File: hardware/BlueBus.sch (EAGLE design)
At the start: 139 parts, among them Q1 NMOSFET-BSS138K, Q2 PMOSFET-DMP32D4S, Q3 NMOSFET-BSS138K, X1 CRYSTAL-12MHZ

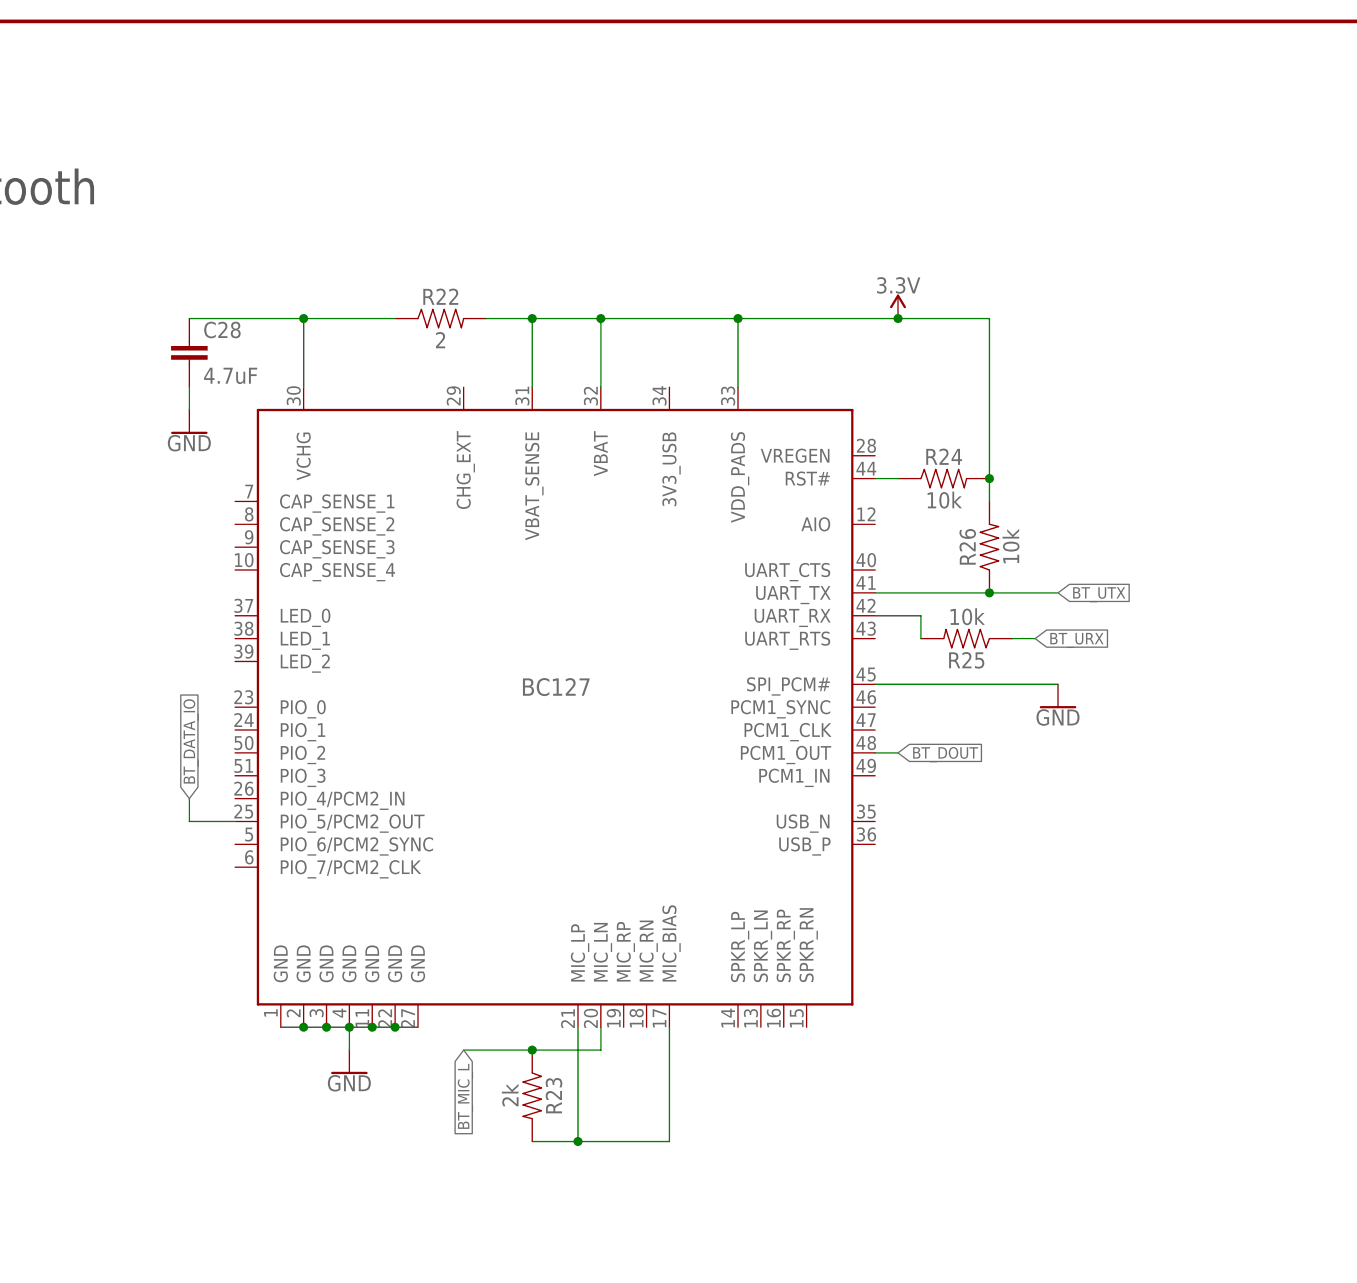
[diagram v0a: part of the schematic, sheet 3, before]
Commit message: [IMP] hardware: v1.1.6 * Re-wire BC127 power input for use with fixed regulated voltage, rather than battery power
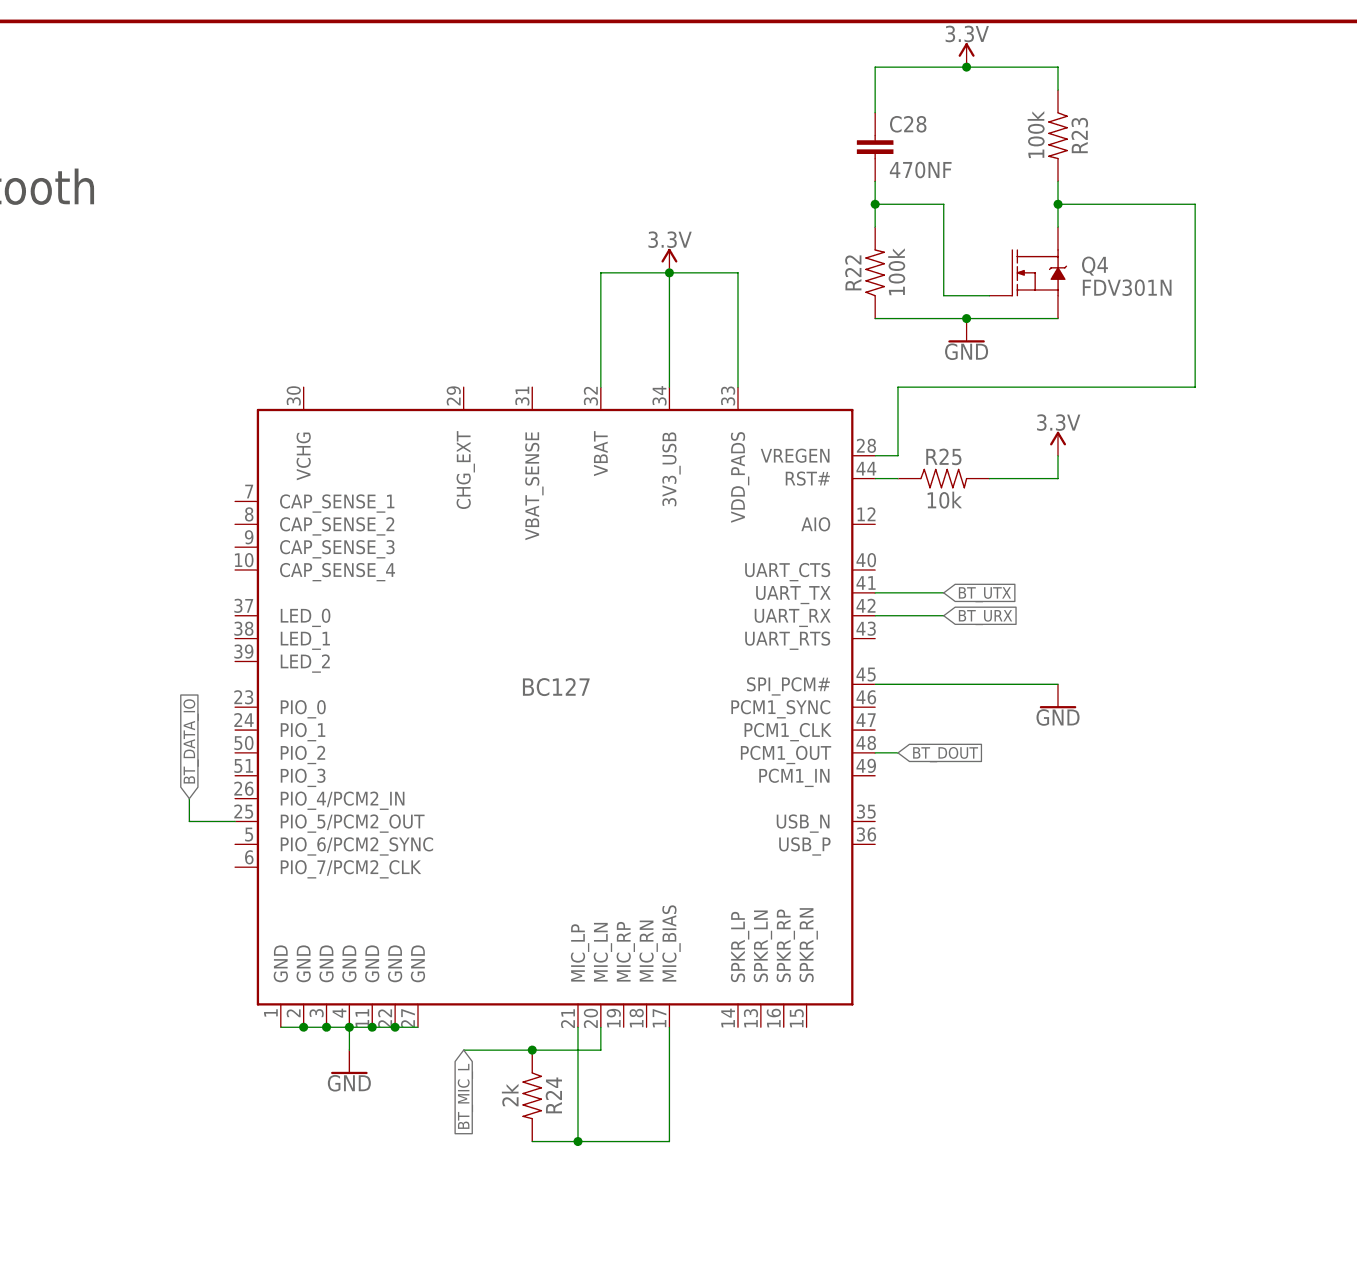
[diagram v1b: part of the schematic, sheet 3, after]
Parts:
- removed R38: 100, Passives:100OHM
- added Q4: FDV301N, Passives:FDV301N
- C28: value 4.7uF -> 470NF; device Passives:4.7UF -> Passives:470NF
- H1, H2, H3, H4: value 2,0-PAD -> 2,2-PAD; device Connectors:2,0-PAD -> Connectors:2,2-PAD
- R22: value 2 -> 100k; device Passives:2OHM -> Passives:100KOHM
- R23: value 2k -> 100k; device Passives:2KOHM -> Passives:100KOHM
- R24: value 10k -> 2k; device Passives:10KOHM -> Passives:2KOHM
- R26: value 10k -> 110; device Passives:10KOHM -> Passives:110OHM
- R27: value 110 -> 210; device Passives:110OHM -> Passives:210OHM
- R28: value 210 -> 10k; device Passives:210OHM -> Passives:10KOHM
- R29, R31: value 10k -> 4.7k; device Passives:10KOHM -> Passives:4.7KOHM
- R30, R32: value 4.7k -> 10k; device Passives:4.7KOHM -> Passives:10KOHM
- R33: value 10k -> 75; device Passives:10KOHM -> Passives:75OHM
- R34: value 75 -> 4.7k; device Passives:75OHM -> Passives:4.7KOHM
- R35: value 4.7k -> 18k; device Passives:4.7KOHM -> Passives:18KOHM
- R36: value 18k -> 100; device Passives:18KOHM -> Passives:100OHM
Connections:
- removed net BT_3V3_FILTER: BC127.VCHG, C28.1, R22.1
- removed net BT_URX_RES: BC127.UART_RX, R25.2
- new net BT_VREGEN: BC127.VREGEN, Q4.D, R23.2
- new net BT_VREGEN_CAP_GATE: C28.2, Q4.G, R22.2
- net 12V: now also R34.1; no longer R35.1
- net 3.3V: now also BC127.3V3_USB, C28.1, R23.1, R25.2, R28.1, R31.1; no longer BC127.VBAT_SENSE, R22.2, R24.2, R26.2, R30.1, R32.1
- net BT_DOUT: now also R33.2; no longer R34.2
- net BT_MIC_BIAS: now also R24.2; no longer R23.2
- net BT_MIC_L: now also R24.1; no longer R23.1
- net BT_RST: now also R25.1; no longer R24.1
- net BT_URX: now also BC127.UART_RX; no longer R25.1
- net BT_UTX: no longer R26.1
- net DAC_OUT_L: now also R37.1; no longer R38.1
- net DAC_OUT_R: now also R36.1; no longer R37.1
- net GND: now also Q4.S, R22.1, R26.1, R30.1, R32.1; no longer C28.2, R27.1, R31.1, R34.1
- net MCU_SCK3: now also R31.2; no longer R32.2
- net MCU_SDA3: now also R29.2; no longer R30.2
- net SPKR_OUT_L: now also R37.2; no longer R38.2
- net SPKR_OUT_R: now also R36.2; no longer R37.2
- net TEL_AMP_INL: now also R35.2; no longer R36.2
- net TEL_AMP_INL_CAP_RES: now also R35.1; no longer R36.1
- net TEL_MIC_L_OUT: now also R34.2; no longer R35.2
- net WM_CSB: now also R32.2; no longer R33.2
- net WM_GPO0: now also R30.2; no longer R31.2
- net WM_RESETB: now also R28.2; no longer R29.2
- net WM_SPDIF_TX_RES: now also R27.2; no longer R28.2
- net WM_SPDIF_TX_RES2: now also R26.2, R27.1; no longer R27.2, R28.1
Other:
- moved on the sheet: C28, R22, R23, R24, R25, R27, R28, R29, R30, R31, R32, R33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

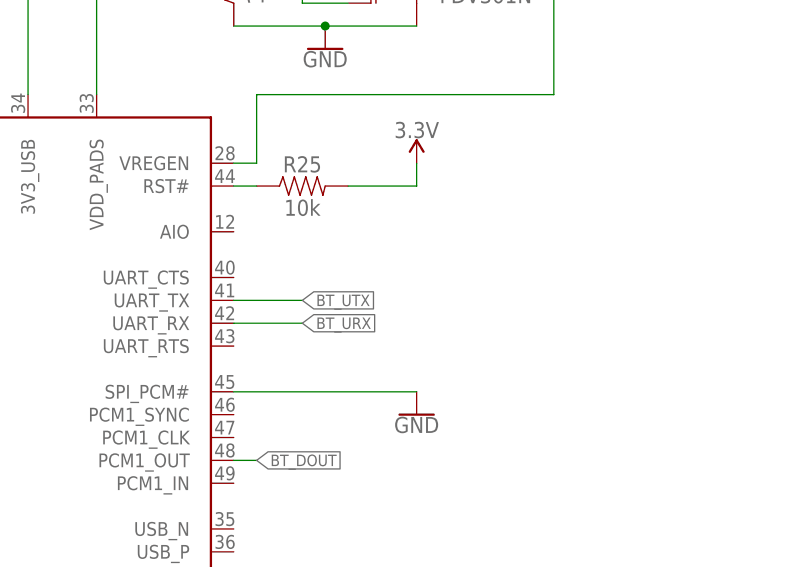
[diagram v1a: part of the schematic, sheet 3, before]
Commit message: [IMP] hardware: v1.6: Minor updates * Re-add 10k resistors to BC127 UART lines * Minor rewiring work around the TMUX154
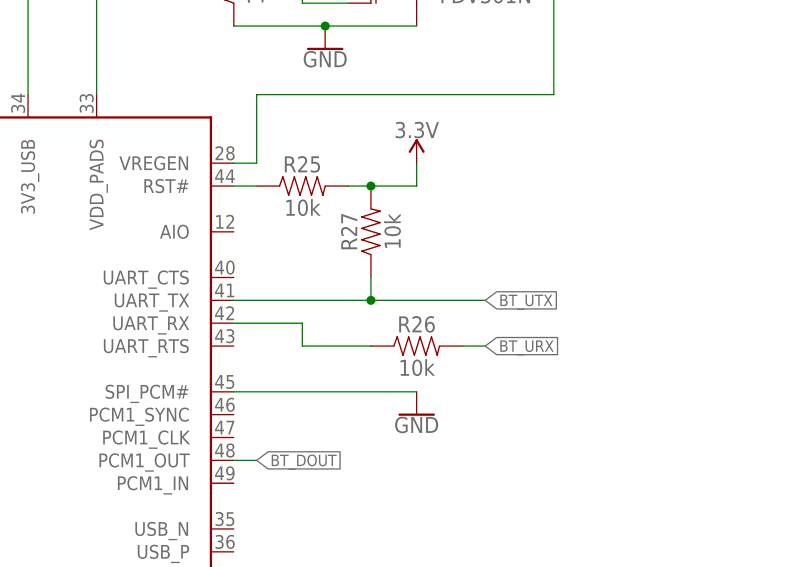
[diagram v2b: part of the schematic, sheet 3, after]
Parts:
- added R38, R39: 100, Passives:100OHM
- R26: value 110 -> 10k; device Passives:110OHM -> Passives:10KOHM
- R27: value 210 -> 10k; device Passives:210OHM -> Passives:10KOHM
- R28: value 10k -> 110; device Passives:10KOHM -> Passives:110OHM
- R29: value 4.7k -> 210; device Passives:4.7KOHM -> Passives:210OHM
- R33: value 75 -> 4.7k; device Passives:75OHM -> Passives:4.7KOHM
- R34: value 4.7k -> 10k; device Passives:4.7KOHM -> Passives:10KOHM
- R35: value 18k -> 75; device Passives:18KOHM -> Passives:75OHM
- R36: value 100 -> 4.7k; device Passives:100OHM -> Passives:4.7KOHM
- R37: value 100 -> 18k; device Passives:100OHM -> Passives:18KOHM
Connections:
- new net BT_URX_RES: BC127.UART_RX, R26.1
- net 12V: now also R36.1; no longer R34.1
- net 3.3V: now also R27.2, R30.1, R33.1; no longer R28.1, R29.1
- net BT_DOUT: now also R35.2; no longer R33.2
- net BT_URX: now also R26.2; no longer BC127.UART_RX
- net BT_UTX: now also R27.1
- net DAC_OUT_L: now also R39.1; no longer R37.1
- net DAC_OUT_R: now also R38.1; no longer R36.1
- net GND: now also R28.1, R34.1, R35.1; no longer R26.1, R30.1, R33.1
- net MCU_SCK3: now also R33.2; no longer R31.2
- net MCU_SDA3: now also R31.2; no longer R29.2
- net SPKR_OUT_L: now also R39.2; no longer R37.2
- net SPKR_OUT_R: now also R38.2; no longer R36.2
- net TEL_AMP_INL: now also R37.2; no longer R35.2
- net TEL_AMP_INL_CAP_RES: now also R37.1; no longer R35.1
- net TEL_MIC_L_OUT: now also R36.2; no longer R34.2
- net WM_CSB: now also R34.2; no longer R32.2
- net WM_GPO0: now also R32.2; no longer R30.2
- net WM_RESETB: now also R30.2; no longer R28.2
- net WM_SPDIF_TX_RES: now also R29.2; no longer R27.2
- net WM_SPDIF_TX_RES2: now also R28.2, R29.1; no longer R26.2, R27.1
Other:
- moved on the sheet: R28, R29, R30, R31, R32, R33, R35, R37
